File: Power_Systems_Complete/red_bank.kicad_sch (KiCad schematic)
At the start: 64 parts

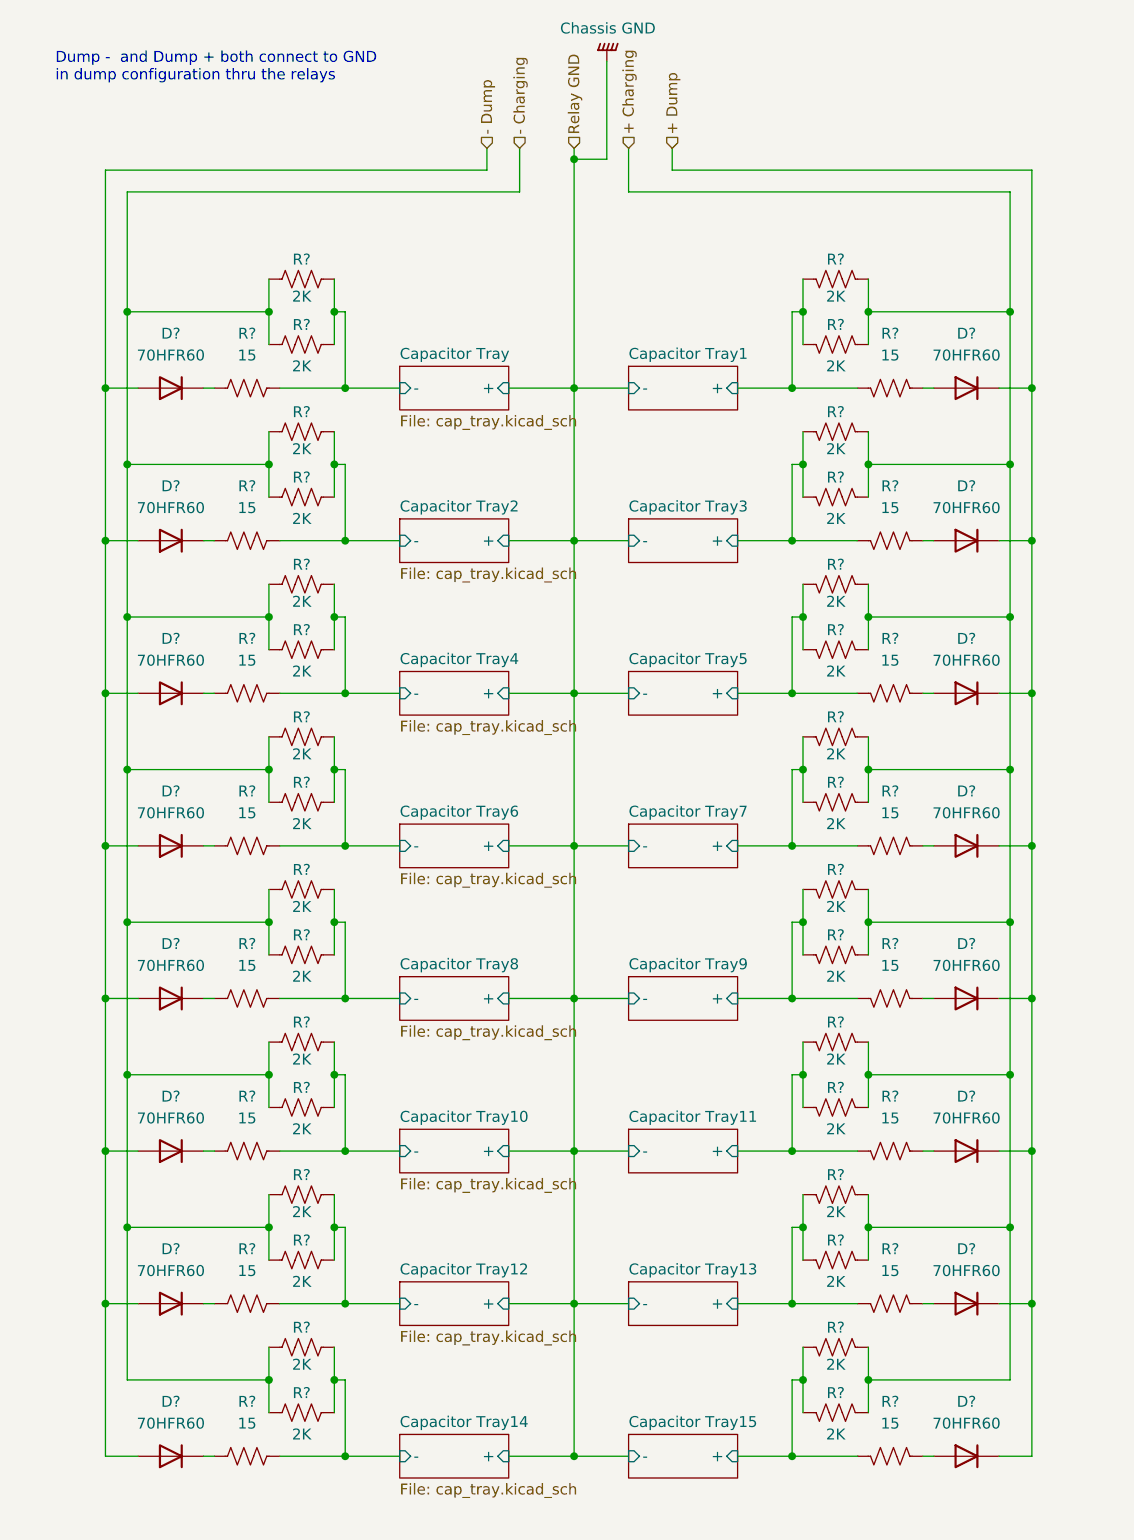
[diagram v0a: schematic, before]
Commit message: Added SPA to complete schematic
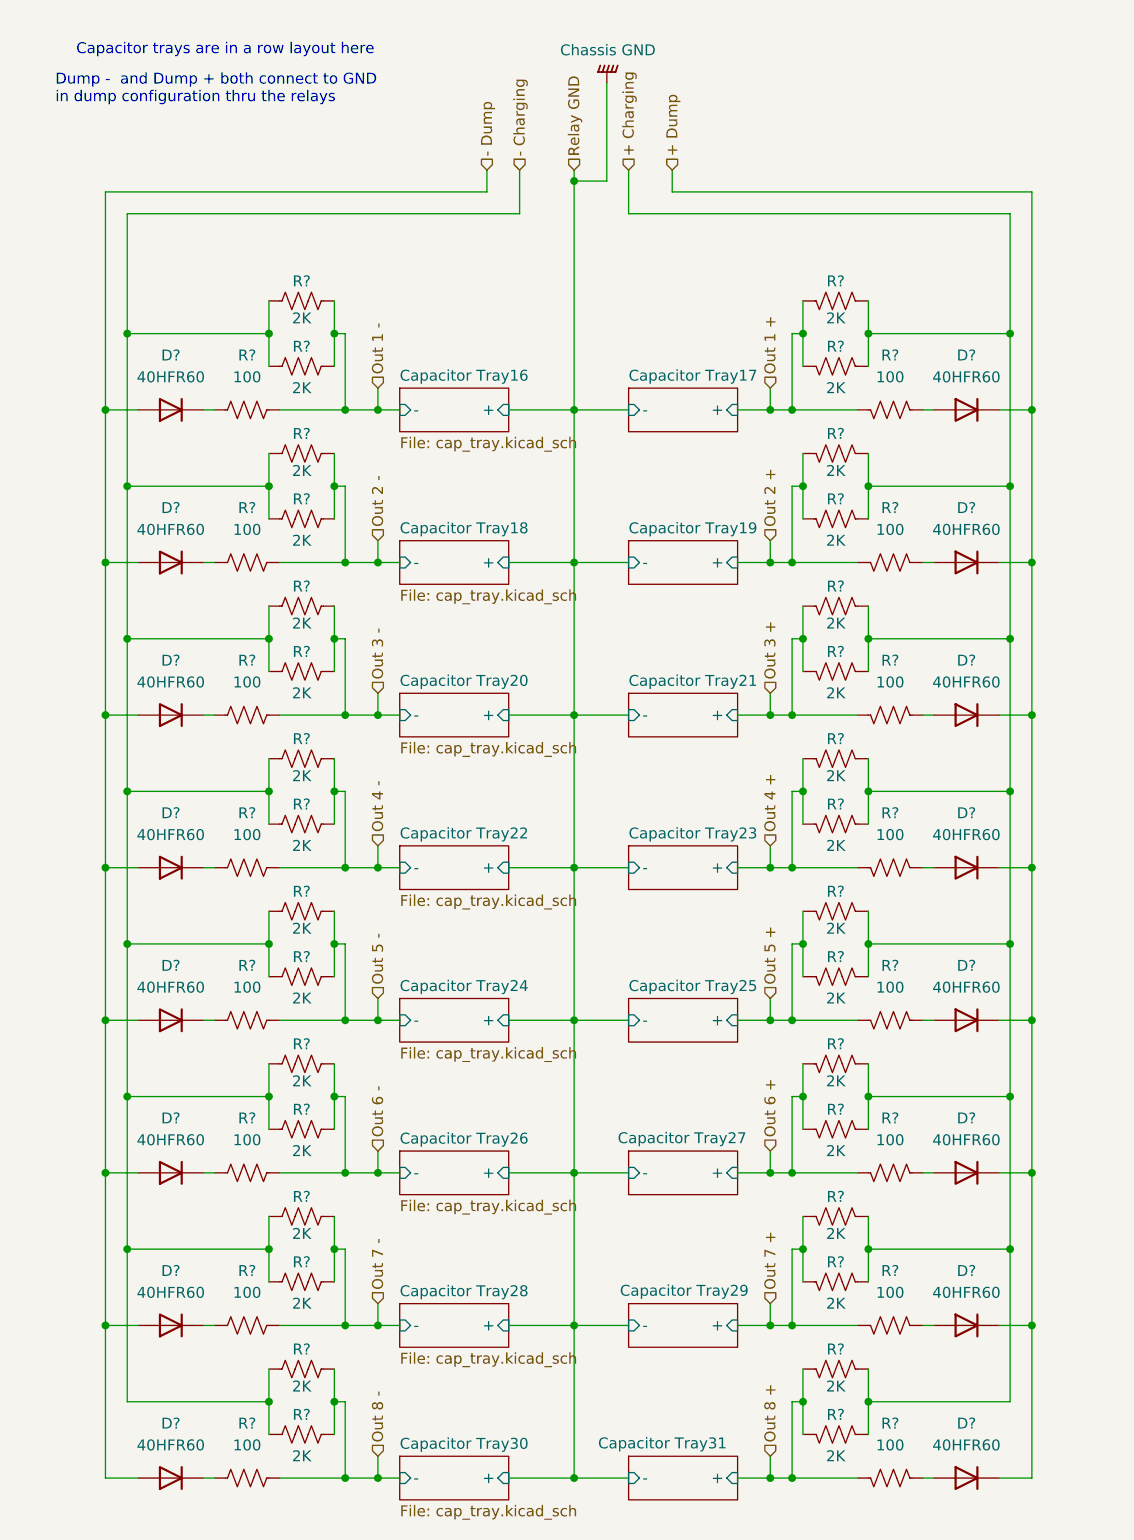
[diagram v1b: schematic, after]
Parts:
- removed D? (x16): 70HFR60, symbol Device:D
- removed R? (x32): 2K, symbol Device:R_US
- removed R? (x16): 15, symbol Device:R_US
- added D? (x16): 40HFR60, symbol Device:D
- added R? (x32): 2K, symbol Device:R_US
- added R? (x16): 100, symbol Device:R_US
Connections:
- net + Charging: now also R?.1, R?.1, R?.1, R?.1, R?.1, R?.1, R?.1, R?.1, R?.1, R?.1, R?.1, R?.1, R?.1, R?.1, R?.1, R?.1
- net + Dump: now also D?.1 (K), D?.1 (K), D?.1 (K), D?.1 (K), D?.1 (K), D?.1 (K), D?.1 (K), D?.1 (K)
- net - Charging: now also R?.1, R?.1, R?.1, R?.1, R?.1, R?.1, R?.1, R?.1, R?.1, R?.1, R?.1, R?.1, R?.1, R?.1, R?.1, R?.1
- net - Dump: now also D?.2 (A), D?.2 (A), D?.2 (A), D?.2 (A), D?.2 (A), D?.2 (A), D?.2 (A), D?.2 (A)
- new net: D?.1 (K), R?.1 (x8)
- new net: D?.2 (A), R?.1 (x8)
- new net Out 1 +: R?.2, R?.2, R?.2
- new net Out 1 -: R?.2, R?.2, R?.2
- new net Out 2 +: R?.2, R?.2, R?.2
- new net Out 2 -: R?.2, R?.2, R?.2
- new net Out 3 +: R?.2, R?.2, R?.2
- new net Out 3 -: R?.2, R?.2, R?.2
- new net Out 4 +: R?.2, R?.2, R?.2
- new net Out 4 -: R?.2, R?.2, R?.2
- new net Out 5 +: R?.2, R?.2, R?.2
- new net Out 5 -: R?.2, R?.2, R?.2
- new net Out 6 +: R?.2, R?.2, R?.2
- new net Out 6 -: R?.2, R?.2, R?.2
- new net Out 7 +: R?.2, R?.2, R?.2
- new net Out 7 -: R?.2, R?.2, R?.2
- new net Out 8 +: R?.2, R?.2, R?.2
- new net Out 8 -: R?.2, R?.2, R?.2
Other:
- removed sheet Capacitor Tray
- removed sheet Capacitor Tray1
- removed sheet Capacitor Tray10
- removed sheet Capacitor Tray11
- removed sheet Capacitor Tray12
- removed sheet Capacitor Tray13
- removed sheet Capacitor Tray14
- removed sheet Capacitor Tray15
- removed sheet Capacitor Tray2
- removed sheet Capacitor Tray3
- removed sheet Capacitor Tray4
- removed sheet Capacitor Tray5
- removed sheet Capacitor Tray6
- removed sheet Capacitor Tray7
- removed sheet Capacitor Tray8
- removed sheet Capacitor Tray9
- added sheet Capacitor Tray16 (cap_tray.kicad_sch)
- added sheet Capacitor Tray17 (cap_tray.kicad_sch)
- added sheet Capacitor Tray18 (cap_tray.kicad_sch)
- added sheet Capacitor Tray19 (cap_tray.kicad_sch)
- added sheet Capacitor Tray20 (cap_tray.kicad_sch)
- added sheet Capacitor Tray21 (cap_tray.kicad_sch)
- added sheet Capacitor Tray22 (cap_tray.kicad_sch)
- added sheet Capacitor Tray23 (cap_tray.kicad_sch)
- added sheet Capacitor Tray24 (cap_tray.kicad_sch)
- added sheet Capacitor Tray25 (cap_tray.kicad_sch)
- added sheet Capacitor Tray26 (cap_tray.kicad_sch)
- added sheet Capacitor Tray27 (cap_tray.kicad_sch)
- added sheet Capacitor Tray28 (cap_tray.kicad_sch)
- added sheet Capacitor Tray29 (cap_tray.kicad_sch)
- added sheet Capacitor Tray30 (cap_tray.kicad_sch)
- added sheet Capacitor Tray31 (cap_tray.kicad_sch)
- note added: "Capacitor trays are in a row layout here"

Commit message: Made changes
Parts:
- added 1N5360B, 1N5360B1, 1N5360B10, 1N5360B13, 1N5360B16, 1N5360B19, 1N5360B22, 1N5360B25, 1N5360B28, 1N5360B31, 1N5360B34, 1N5360B37, 1N5360B4, 1N5360B40, 1N5360B43, 1N5360B7: D_Zener, symbol Device:D_Zener
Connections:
- net Chassis GND: now also 1N5360B.2 (A), 1N5360B1.1 (K), 1N5360B10.2 (A), 1N5360B13.2 (A), 1N5360B16.2 (A), 1N5360B19.2 (A), 1N5360B22.2 (A), 1N5360B25.2 (A), 1N5360B28.1 (K), 1N5360B31.1 (K), 1N5360B34.1 (K), 1N5360B37.1 (K), 1N5360B4.1 (K), 1N5360B40.1 (K), 1N5360B43.1 (K), 1N5360B7.2 (A)
- net Out 1 +: now also 1N5360B1.2 (A)
- net Out 1 -: now also 1N5360B.1 (K)
- net Out 2 +: now also 1N5360B4.2 (A)
- net Out 2 -: now also 1N5360B7.1 (K)
- net Out 3 +: now also 1N5360B28.2 (A)
- net Out 3 -: now also 1N5360B10.1 (K)
- net Out 4 +: now also 1N5360B31.2 (A)
- net Out 4 -: now also 1N5360B13.1 (K)
- net Out 5 +: now also 1N5360B34.2 (A)
- net Out 5 -: now also 1N5360B16.1 (K)
- net Out 6 +: now also 1N5360B37.2 (A)
- net Out 6 -: now also 1N5360B19.1 (K)
- net Out 7 +: now also 1N5360B40.2 (A)
- net Out 7 -: now also 1N5360B22.1 (K)
- net Out 8 +: now also 1N5360B43.2 (A)
- net Out 8 -: now also 1N5360B25.1 (K)

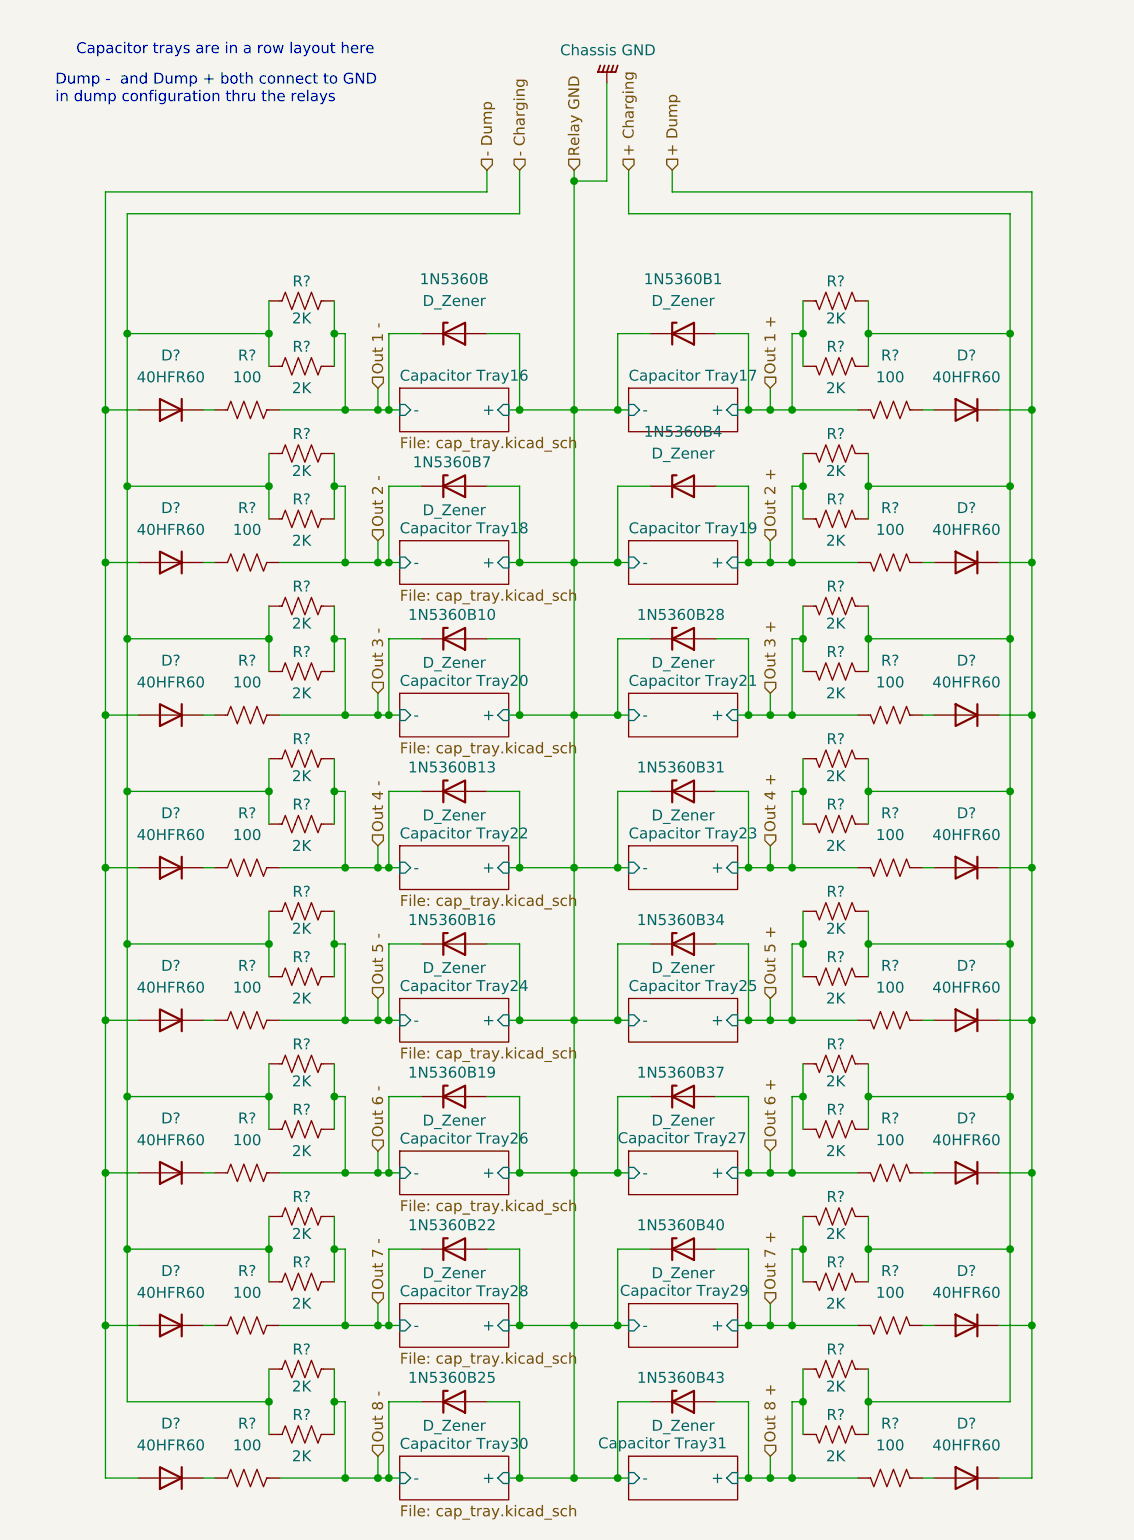
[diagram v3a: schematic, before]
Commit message: Edited red cap bank 1 caps
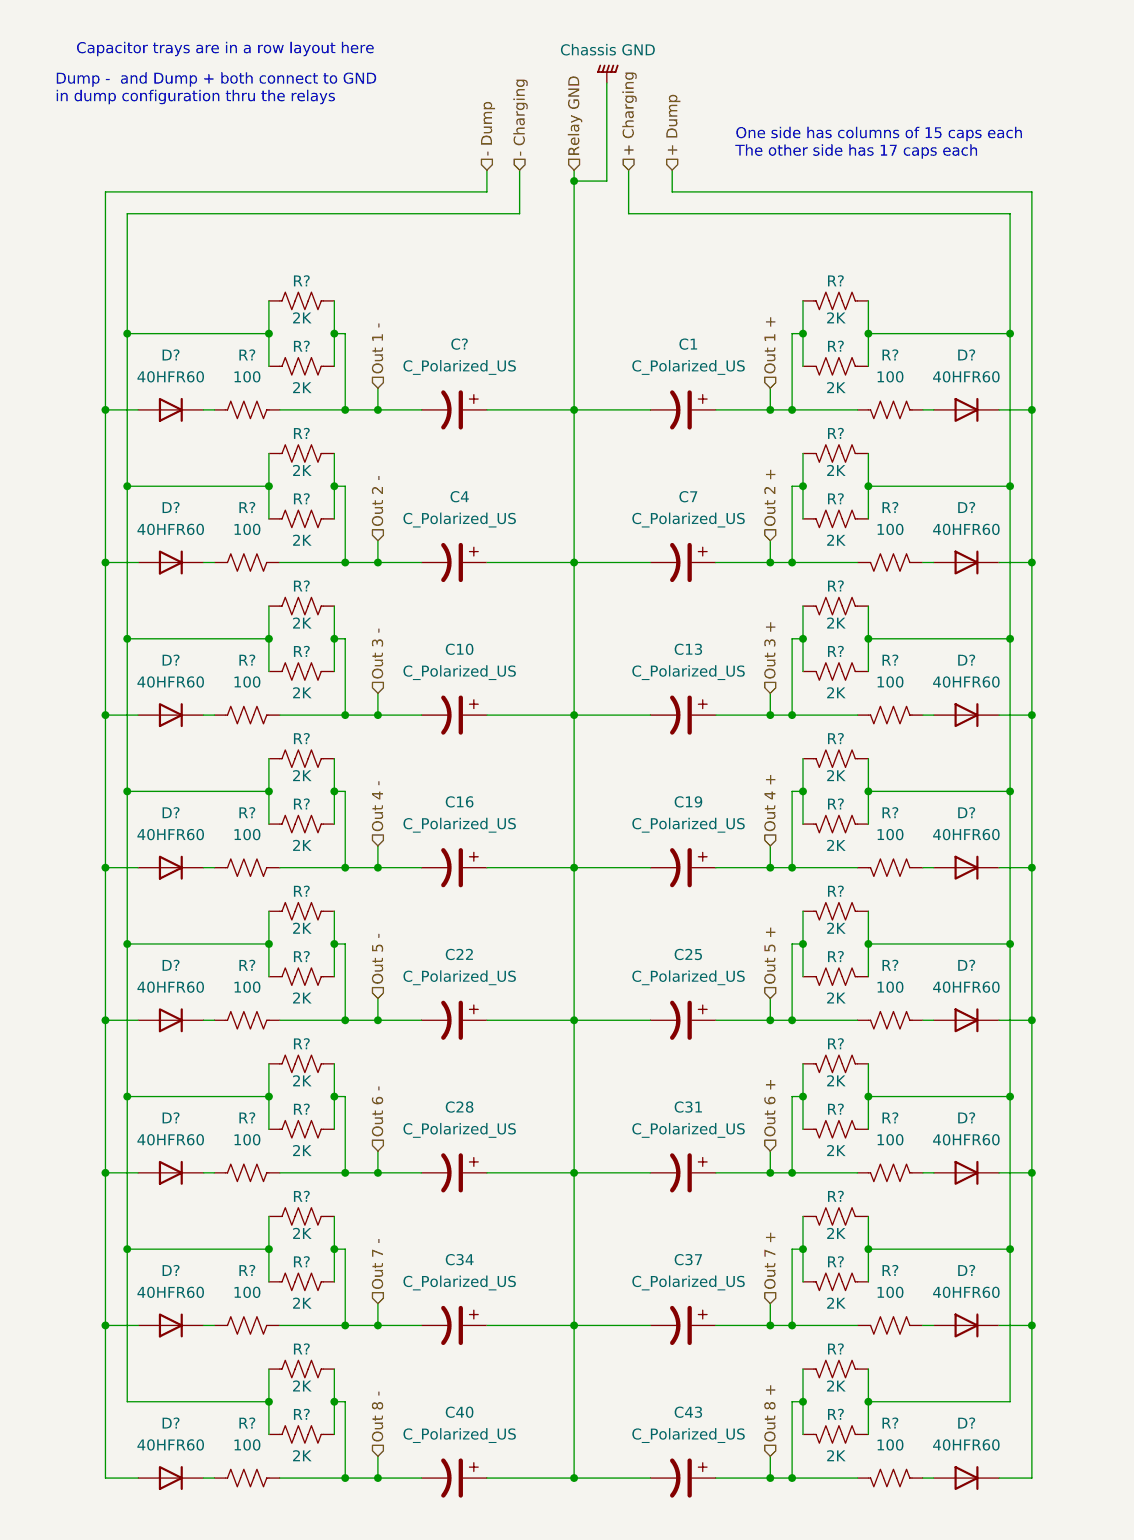
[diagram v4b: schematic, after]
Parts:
- removed 1N5360B, 1N5360B1, 1N5360B10, 1N5360B13, 1N5360B16, 1N5360B19, 1N5360B22, 1N5360B25, 1N5360B28, 1N5360B31, 1N5360B34, 1N5360B37, 1N5360B4, 1N5360B40, 1N5360B43, 1N5360B7: D_Zener, symbol Device:D_Zener
- added C1, C10, C13, C16, C19, C22, C25, C28, C31, C34, C37, C4, C40, C43, C7, C?: C_Polarized_US, symbol Device:C_Polarized_US
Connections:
- net Chassis GND: now also C1.2, C10.1, C13.2, C16.1, C19.2, C22.1, C25.2, C28.1, C31.2, C34.1, C37.2, C4.1, C40.1, C43.2, C7.2, C?.1
- net Out 1 +: now also C1.1
- net Out 1 -: now also C?.2
- net Out 2 +: now also C7.1
- net Out 2 -: now also C4.2
- net Out 3 +: now also C13.1
- net Out 3 -: now also C10.2
- net Out 4 +: now also C19.1
- net Out 4 -: now also C16.2
- net Out 5 +: now also C25.1
- net Out 5 -: now also C22.2
- net Out 6 +: now also C31.1
- net Out 6 -: now also C28.2
- net Out 7 +: now also C37.1
- net Out 7 -: now also C34.2
- net Out 8 +: now also C43.1
- net Out 8 -: now also C40.2
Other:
- removed sheet Capacitor Tray16
- removed sheet Capacitor Tray17
- removed sheet Capacitor Tray18
- removed sheet Capacitor Tray19
- removed sheet Capacitor Tray20
- removed sheet Capacitor Tray21
- removed sheet Capacitor Tray22
- removed sheet Capacitor Tray23
- removed sheet Capacitor Tray24
- removed sheet Capacitor Tray25
- removed sheet Capacitor Tray26
- removed sheet Capacitor Tray27
- removed sheet Capacitor Tray28
- removed sheet Capacitor Tray29
- removed sheet Capacitor Tray30
- removed sheet Capacitor Tray31
- note added: "One side has columns of 15 caps each The other side has 17 caps each"
